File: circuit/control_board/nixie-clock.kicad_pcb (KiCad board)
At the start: 2 copper layers, 38 parts, among them IC1 ATMEGA328-P, P1 CONN_2, P2 CONN_2, P3 CONN_4, P4 CONN_4, P5 CONN_8, P6 CONN_12, P7 CONN_2, P8 CONN_2, Q1 NPN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

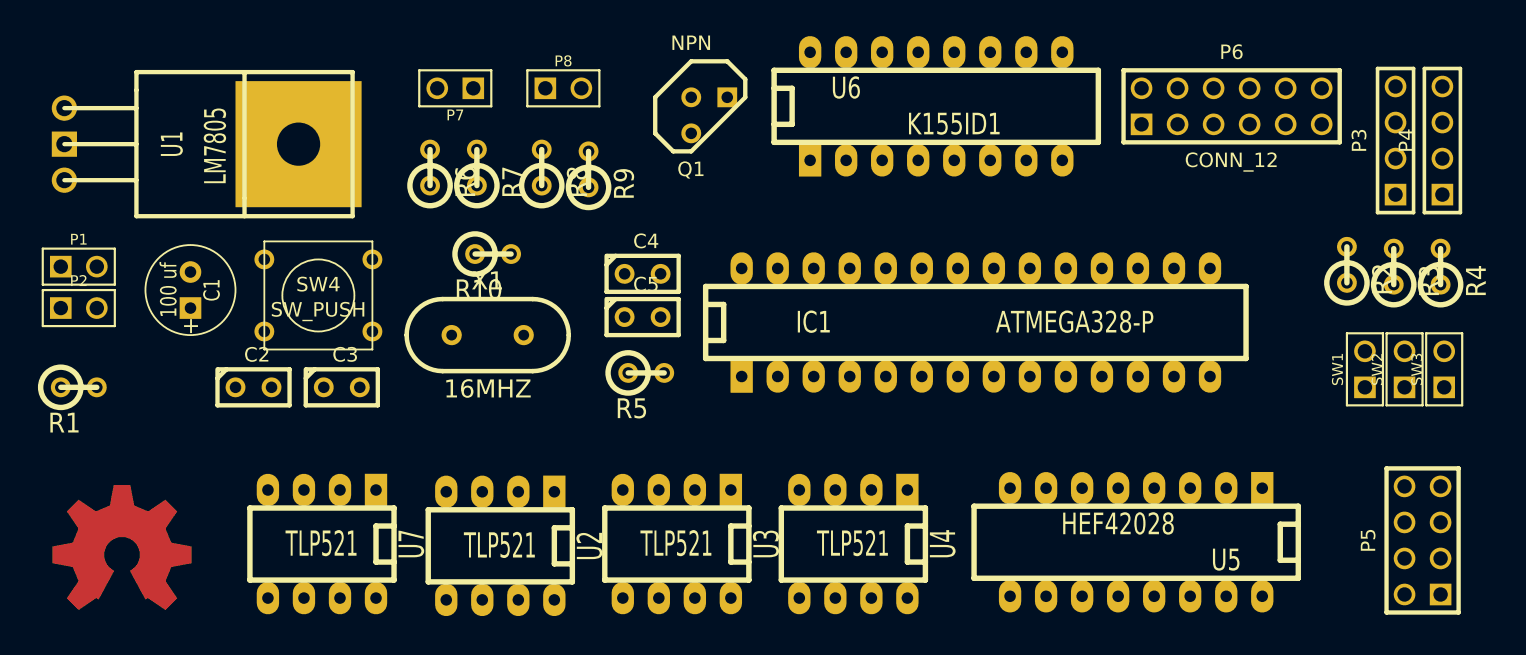
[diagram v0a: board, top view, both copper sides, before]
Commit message: Control board: Create the PCB zone
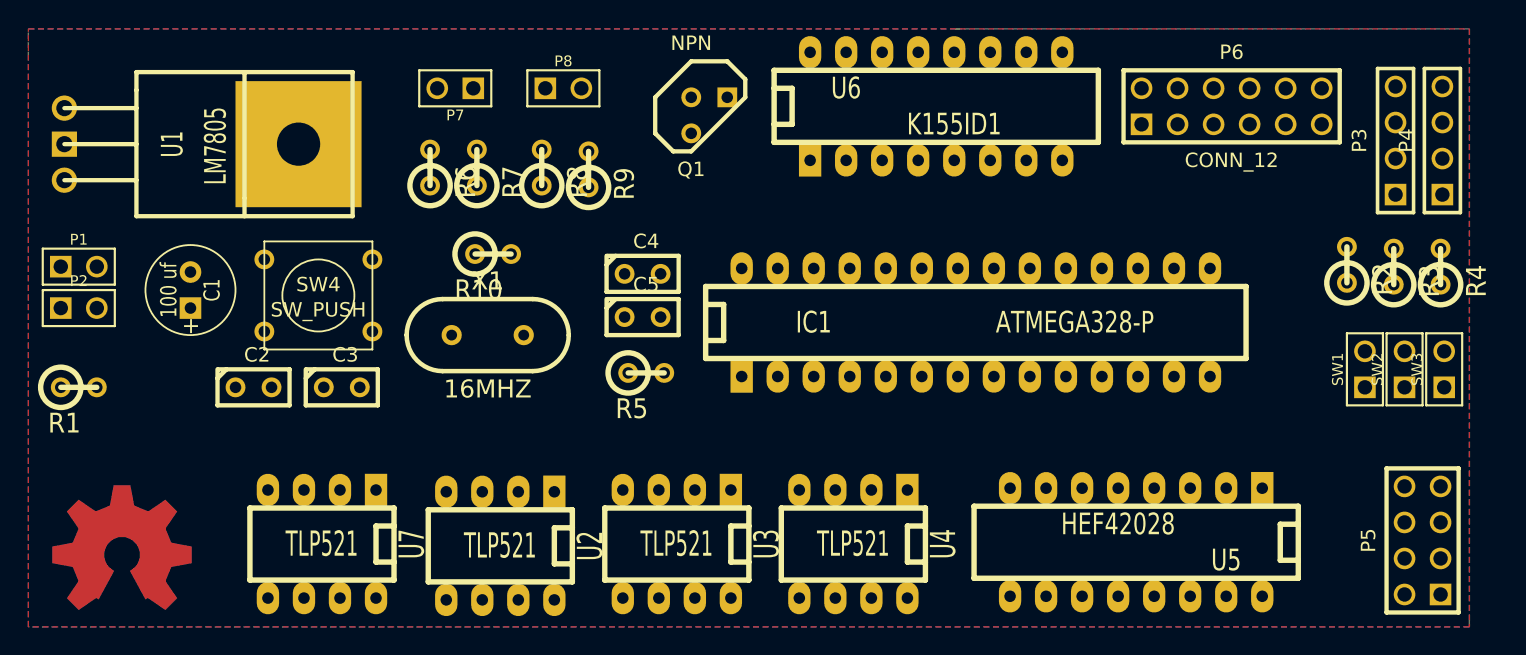
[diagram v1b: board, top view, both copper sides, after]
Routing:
- added copper zone on B.Cu, net (none)
- added copper zone on F.Cu, net (none)
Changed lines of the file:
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@@
     (last_trace_width 0.254)
     (trace_clearance 0.254)
-    (zone_clearance 0.508)
+    (zone_clearance 1)
     (zone_45_only no)
     (trace_min 0.254)
@@
     )
   )
+  (zone (net 0) (net_name "") (layer B.Cu) (hatch edge 0.508)
+    (connect_pads (clearance 1))
+    (min_thickness 0.254)
+    (fill (arc_segments 16) (thermal_gap 0.508) (thermal_bridge_width 0.508))
+    (polygon
+      (pts
+        (xy 138.938 46.228) (xy 175.26 46.228) (xy 175.26 87.884) (xy 175.26 88.392) (xy 108.204 88.392)
+        (xy 73.66 88.392) (xy 73.66 48.26) (xy 73.66 46.228) (xy 139.446 46.228)
+      )
+    )
+  )
+  (zone (net 0) (net_name "") (layer F.Cu) (hatch edge 0.508)
+    (connect_pads (clearance 1))
+    (min_thickness 0.254)
+    (fill (arc_segments 16) (thermal_gap 0.508) (thermal_bridge_width 0.508))
+    (polygon
+      (pts
+        (xy 175.26 88.392) (xy 73.66 88.392) (xy 73.66 46.228) (xy 175.26 46.228)
+      )
+    )
+  )

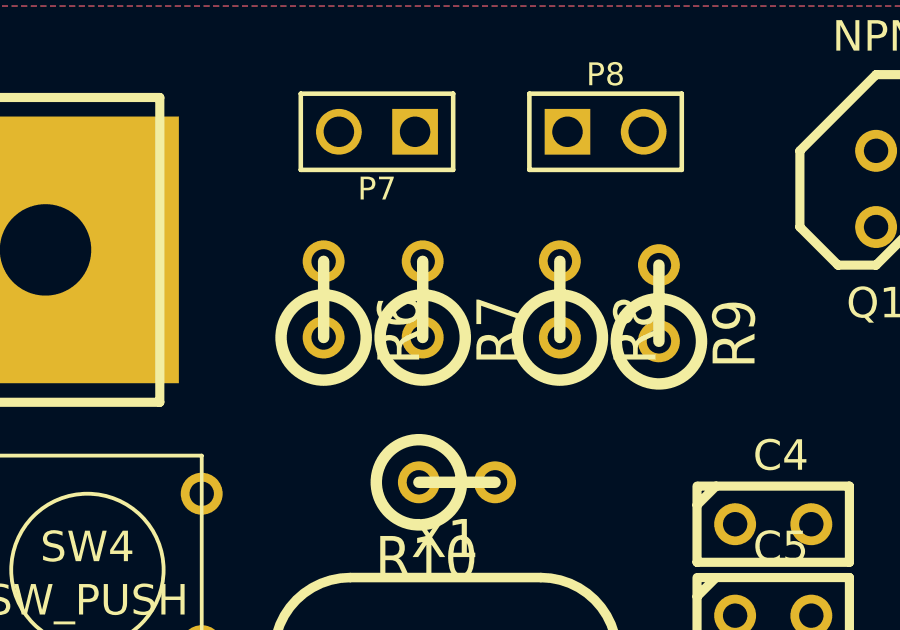
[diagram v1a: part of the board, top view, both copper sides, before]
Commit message: Control board: Adjust the wire
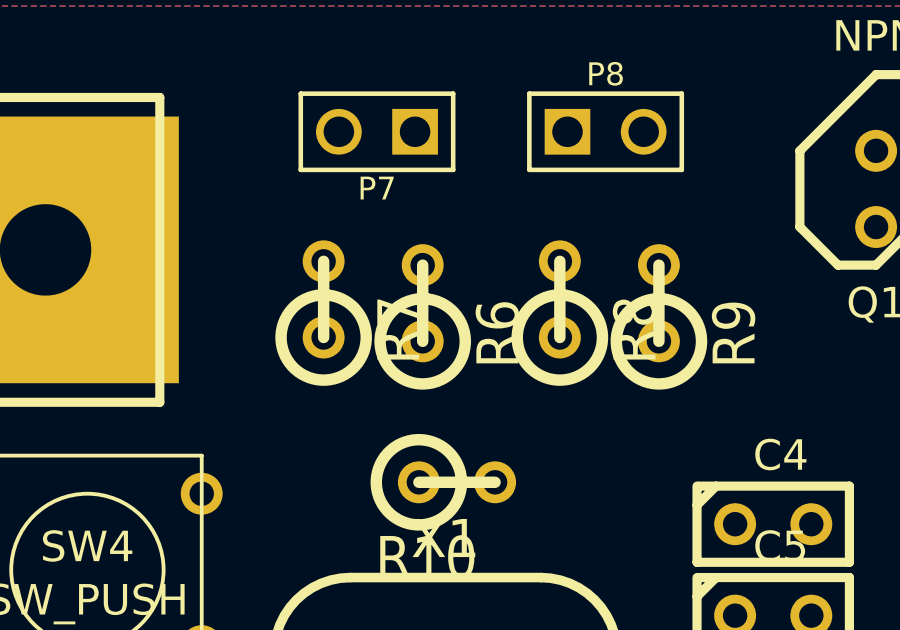
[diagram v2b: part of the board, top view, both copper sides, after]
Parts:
- moved R6 3.30 mm to (105.3, 56.1)
- moved R7 3.30 mm to (102.0, 56.0)
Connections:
- U2 pad 6: N-0000026 -> 170V
- U2 pad 8: N-0000026 -> 170V
- U3 pad 6: N-0000026 -> 170V
- U3 pad 8: N-0000026 -> 170V
- U4 pad 6: N-0000026 -> 170V
- U4 pad 8: N-0000026 -> 170V
- U7 pad 6: N-0000026 -> 170V
- U7 pad 8: N-0000026 -> 170V

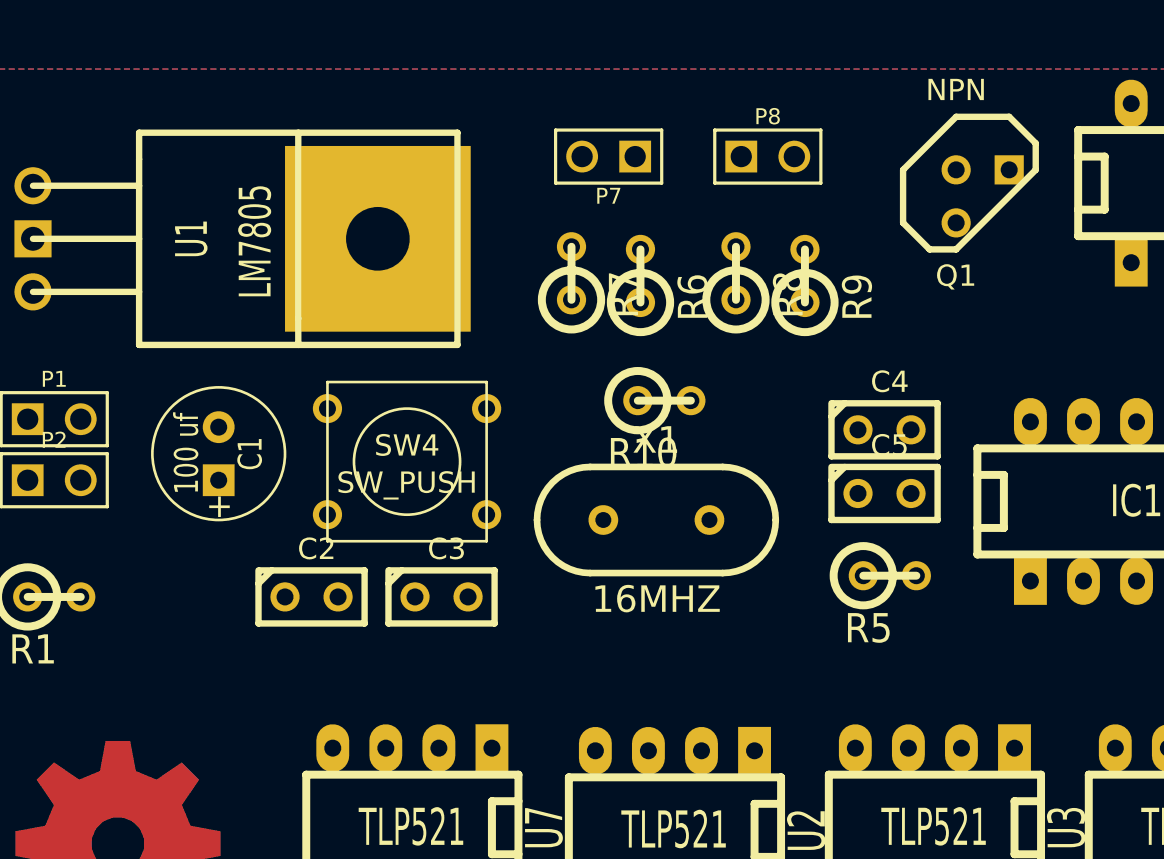
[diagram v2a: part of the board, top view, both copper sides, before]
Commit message: Control board: Update the PCB placement
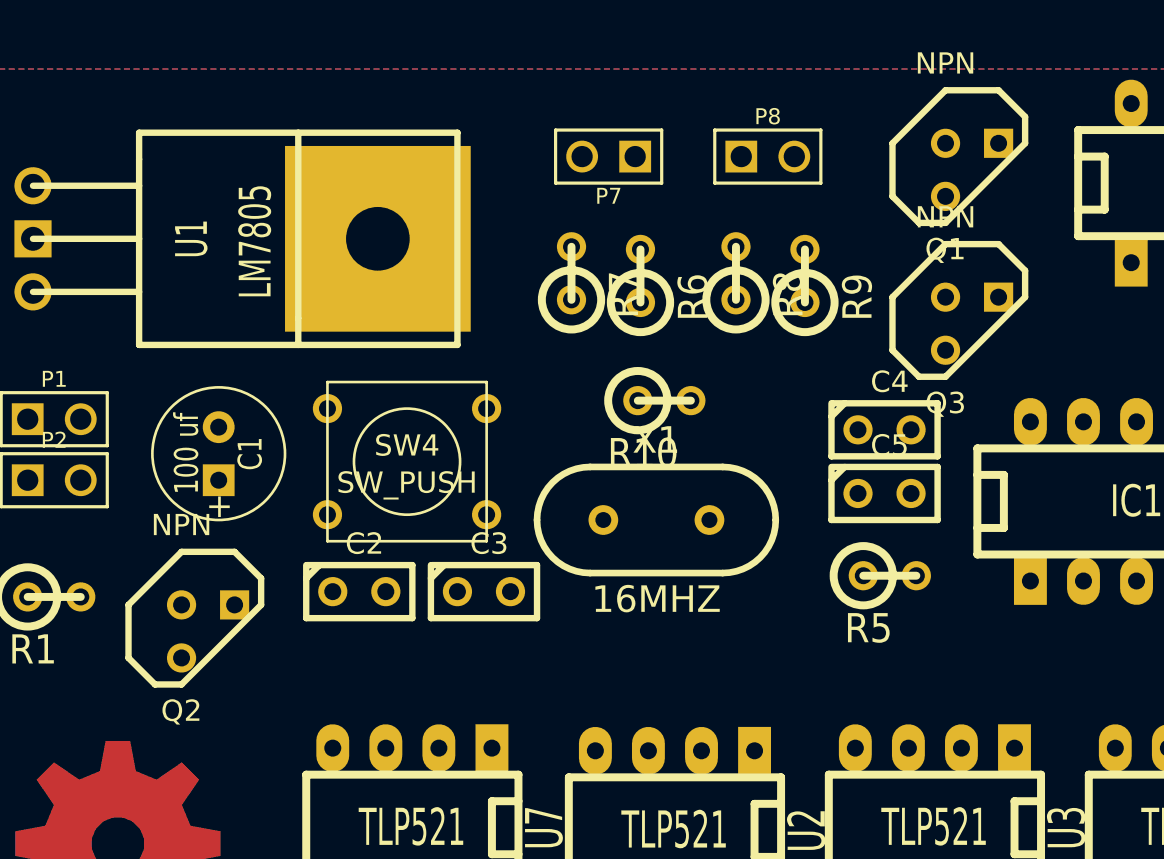
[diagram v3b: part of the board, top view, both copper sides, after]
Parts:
- added Q2: NPN, TO92, F.Cu at (84.6, 73.2)
- added Q3: NPN, TO92, F.Cu at (121.2, 58.4)
- moved C2 2.30 mm to (91.8, 71.2)
- moved C3 2.05 mm to (97.8, 71.2)
- moved Q1 1.37 mm to (121.2, 51.1)
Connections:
- IC1 pad 15: N-0000060 -> Brightness
- IC1 pad 24: N-0000061 -> Left dot
- U2 pad 6: 170V -> N-0000023
- U2 pad 8: 170V -> N-0000023
- U3 pad 6: 170V -> N-0000023
- U3 pad 8: 170V -> N-0000023
- U4 pad 6: 170V -> N-0000023
- U4 pad 8: 170V -> N-0000023
- U7 pad 6: 170V -> N-0000023
- U7 pad 8: 170V -> N-0000023

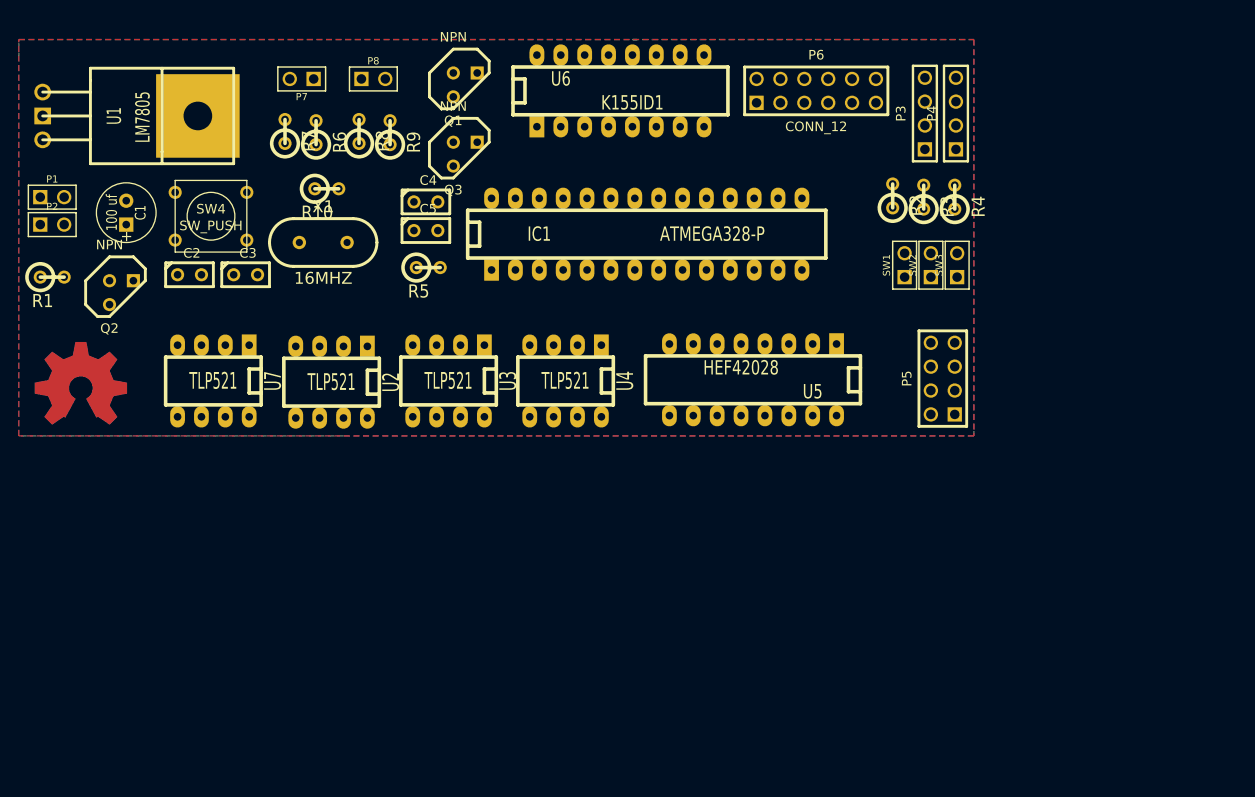
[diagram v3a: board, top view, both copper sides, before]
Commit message: Control board: Autoroute the wire
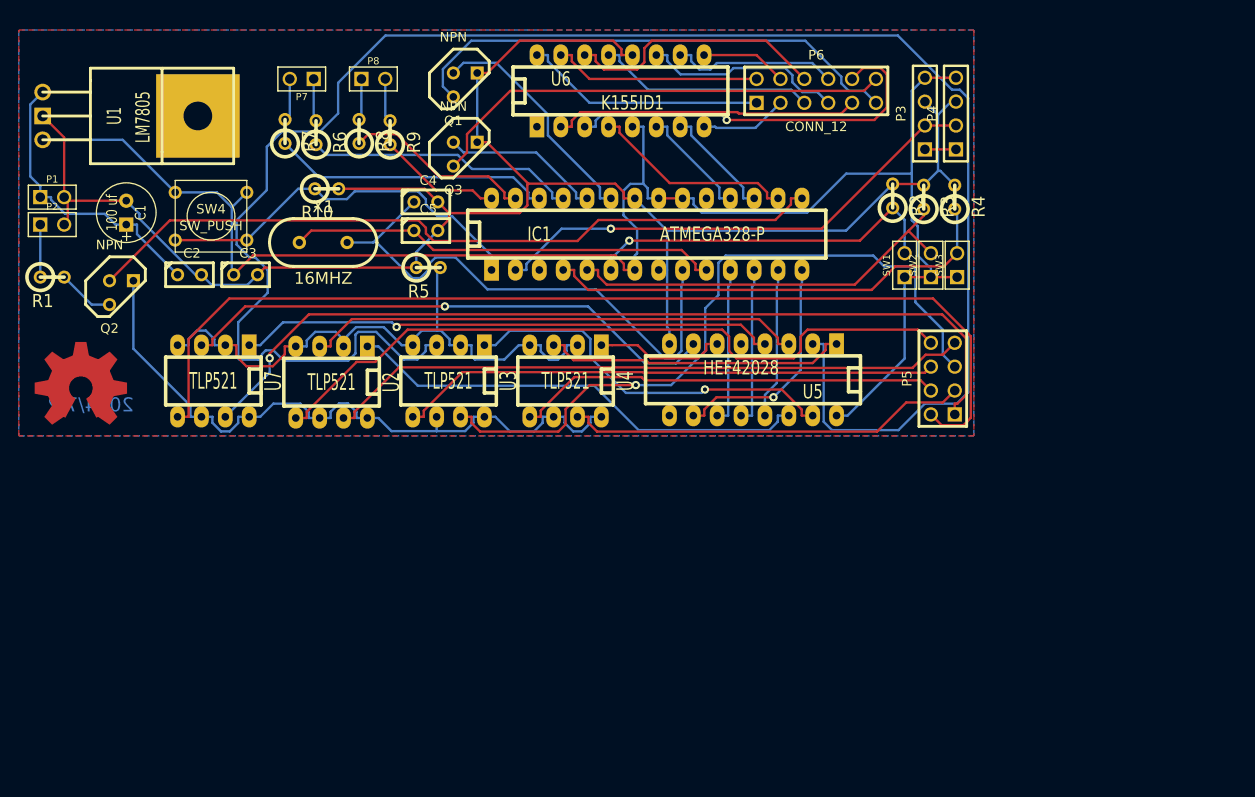
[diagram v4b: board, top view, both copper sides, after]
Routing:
- net N-000005: track 0.00 -> 196.0 mm
- net GND: track 0.00 -> 194.0 mm
- net 5V: track 0.00 -> 178.6 mm
- net N-0000010: track 0.00 -> 109.8 mm
- net N-0000028: track 0.00 -> 94.3 mm, vias 0 -> 1
- net Brightness: track 0.00 -> 79.8 mm
- net N-0000027: track 0.00 -> 76.8 mm
- net N-0000029: track 0.00 -> 75.6 mm, vias 0 -> 1
- net N-0000023: track 0.00 -> 73.2 mm
- net N-0000031: track 0.00 -> 68.8 mm
- net N-0000024: track 0.00 -> 64.1 mm
- net N-000001: track 0.00 -> 57.9 mm, vias 0 -> 1
- net Crystal1: track 0.00 -> 57.8 mm
- net N-0000030: track 0.00 -> 57.8 mm
- net N-0000022: track 0.00 -> 57.4 mm, vias 0 -> 1
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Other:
- board text added: "2014/7/2"

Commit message: Control board: Arrange the circuit and re-autoroute the PCB board
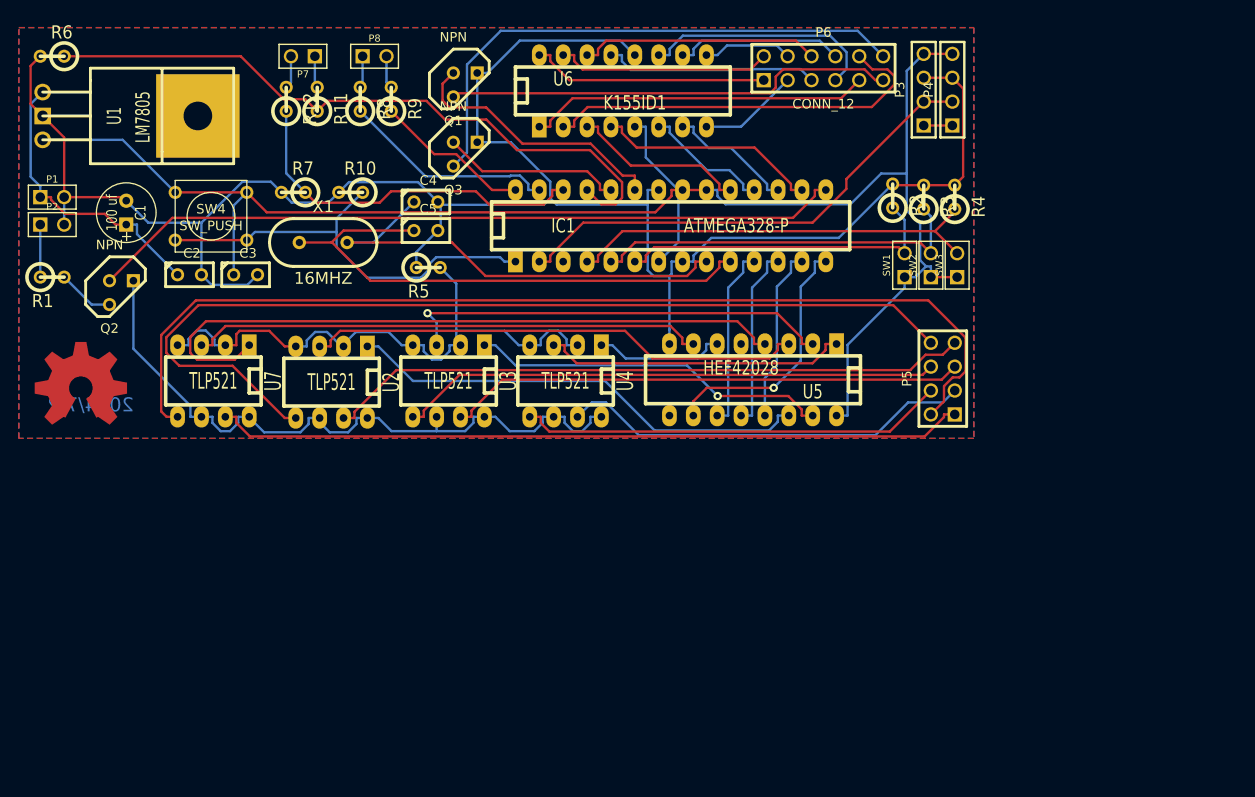
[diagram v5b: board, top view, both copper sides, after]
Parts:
- added R11: 1.8kohm, R1, F.Cu at (105.4, 52.6)
- added R12: 1.8kohm, R1, F.Cu at (102.1, 52.6)
- R6, R7: value 220ohm -> 330ohm
- moved R6 29.2 mm to (77.2, 48.0), turned to 180 degrees
- moved R7 6.54 mm to (102.9, 62.5), turned to 180 degrees
- moved R9 3.56 mm to (113.3, 52.6)
- moved R8 3.43 mm to (110.0, 52.6)
- moved IC1 2.69 mm to (143.0, 66.0)
- moved P4 2.57 mm to (173.0, 51.6)
- moved R10 2.57 mm to (109.0, 62.5), turned to 180 degrees
- moved P3 2.54 mm to (169.9, 51.6)
- moved P6 2.53 mm to (159.3, 49.3)
- moved P7 2.42 mm to (103.9, 48.0)
- moved P8 2.42 mm to (111.5, 48.0)
- moved U6 0.25 mm to (137.9, 51.7)
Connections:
- P6 pad 10: N-0000041 -> N-0000017
- P6 pad 9: N-0000042 -> N-0000018
- P7 pad 1: N-0000063 -> N-0000038
- P7 pad 2: N-0000062 (its old number) -> N-0000037
- R6 pad 2: N-0000063 -> GND
- R7 pad 2: N-0000062 (its old number) -> GND
- U6 pad 1: (no net) -> N-0000018
- U6 pad 2: N-0000042 -> N-0000017
- U6 pad 3: N-0000041 -> Font A
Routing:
- net N-0000051: track 196.0 -> 46.5 mm, vias 0 -> 1
- net MP3 Tx: track 29.0 -> 72.1 mm
- net N-0000017: track 0.00 -> 43.0 mm
- net N-0000041: track 42.0 -> 0.00 mm, vias 1 -> 0
- net N-0000018: track 0.00 -> 36.5 mm
- net N-0000042: track 32.5 -> 0.00 mm
- net N-0000011: track 76.8 -> 102.7 mm
- net GND: track 194.0 -> 216.3 mm
- net N-000008: track 75.6 -> 55.2 mm, vias 1 -> 0
- net Font A: track 0.00 -> 18.8 mm
- net N-0000045: track 57.4 -> 72.1 mm, vias 1 -> 0
- net N-000007: track 94.3 -> 80.0 mm, vias 1 -> 0
- net Crystal2: track 46.0 -> 58.0 mm
- net MP3 Rx: track 29.8 -> 39.5 mm
- net N-0000015: track 49.9 -> 58.3 mm
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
